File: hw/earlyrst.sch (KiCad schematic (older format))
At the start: 7 parts

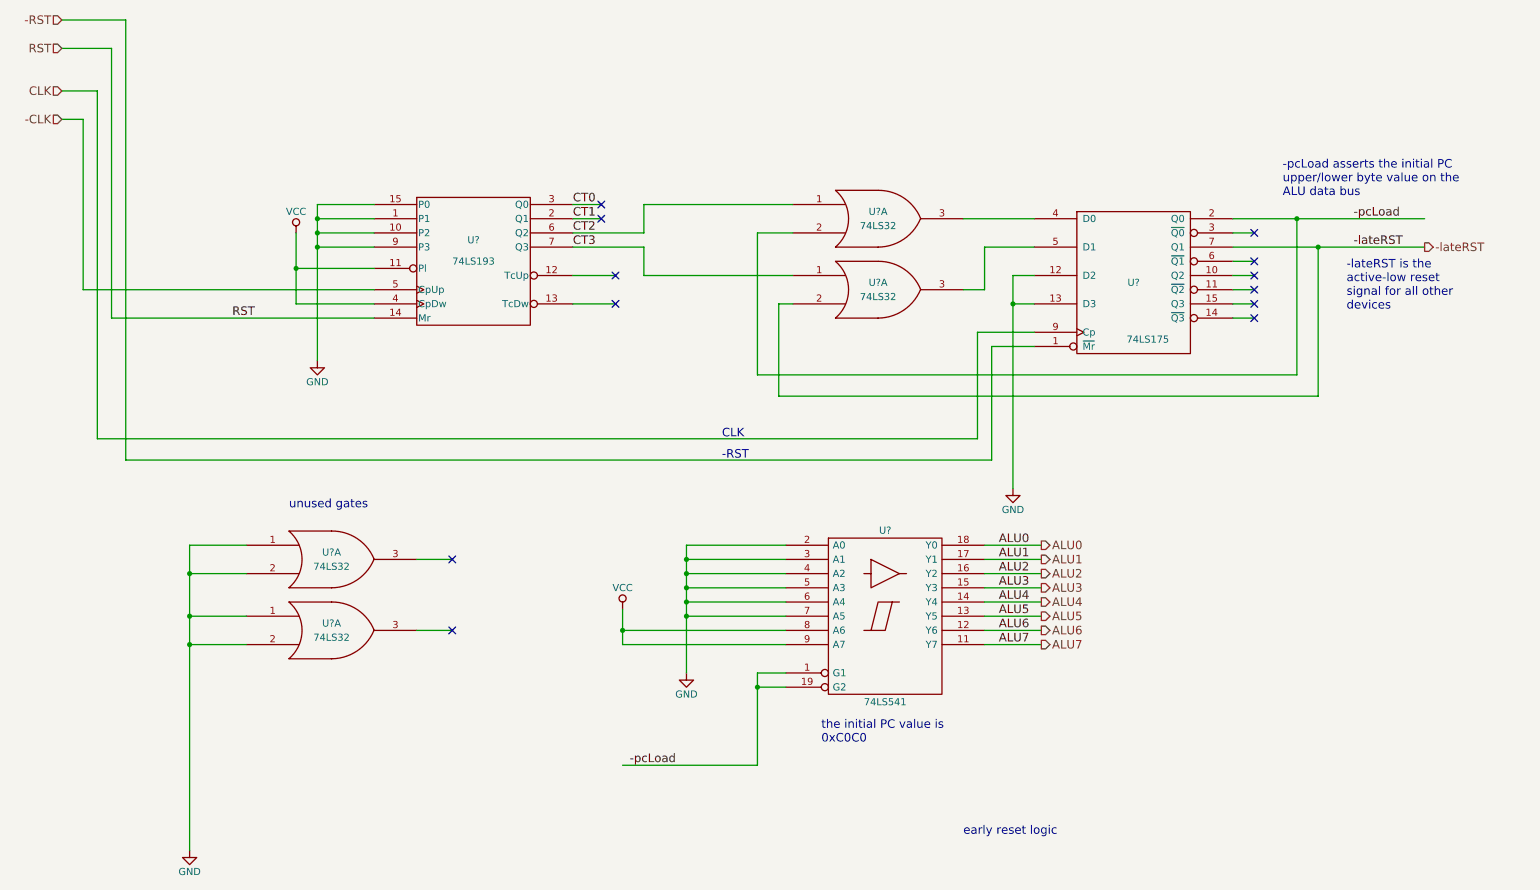
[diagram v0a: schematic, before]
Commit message: redesign of early reset logic
Use a '393 counter to generate delayed high signals for
-wrPC (write the PC high/low registers), -initPC
(assert the initial PC byte value on the ALU data bus),
and -lateRST (reset signal for other components.)

This (hopefully) fixes an issue with the previous design
where the initial PC value was clocked in on the same
clock edge as the one that de-asserted the driving of
the initial PC byte value onto the ALU data bus.
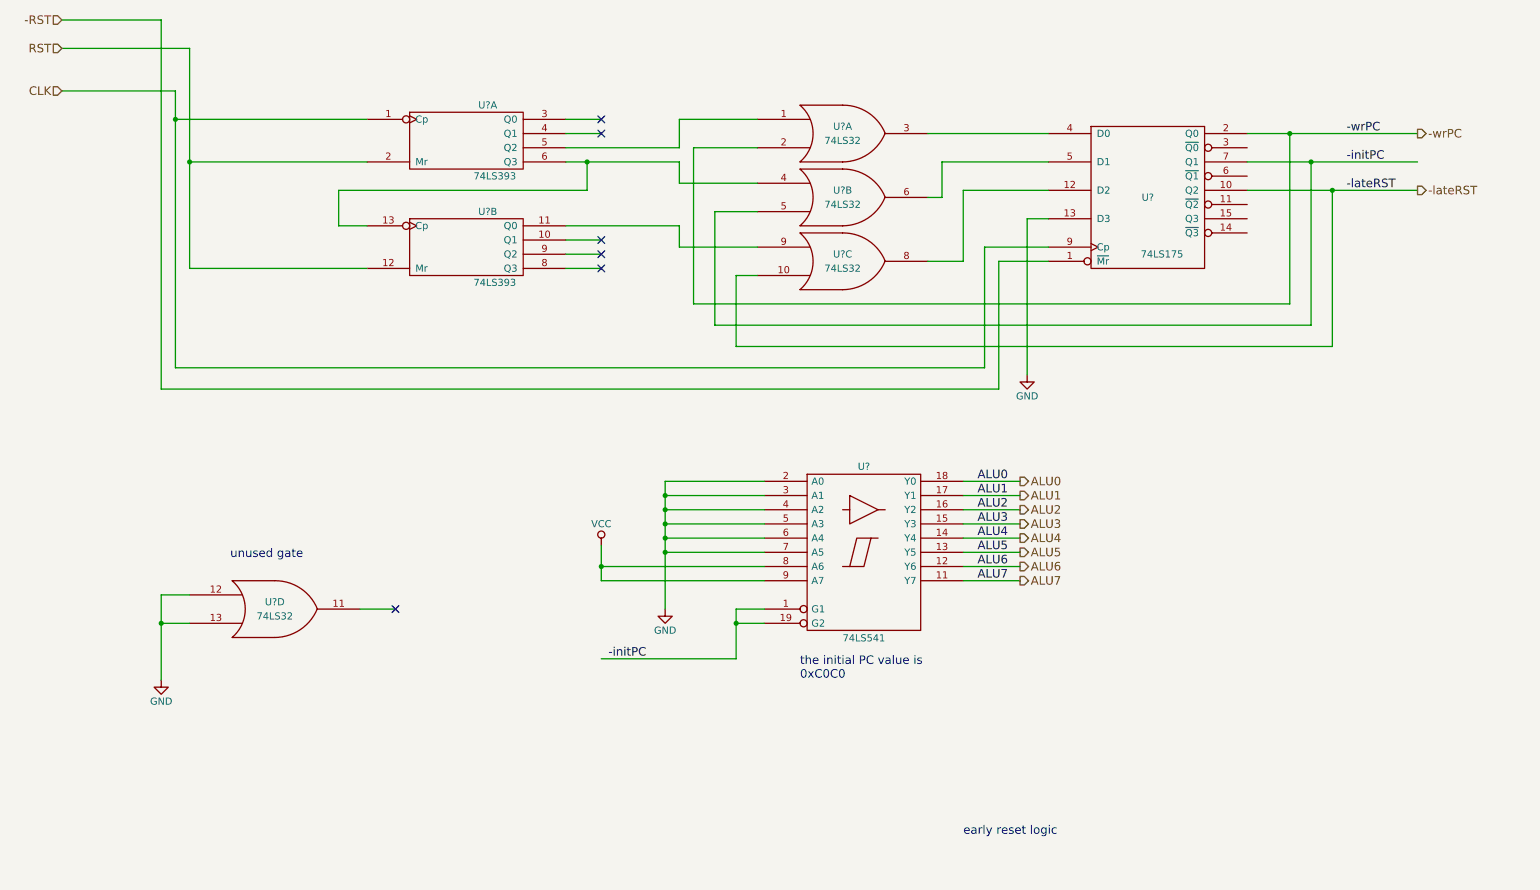
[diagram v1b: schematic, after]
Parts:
- removed U?: 74LS193, symbol 74LS193
- removed U? (x4): 74LS32, symbol 74LS32
- removed U?: 74LS175, symbol 74LS175
- added U? (x2): 74LS393, symbol 74LS393
- added U?: 74LS175, symbol 74LS175
- added U? (x4): 74LS32, symbol 74LS32
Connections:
- net -RST: now also U?.1 (~Mr)
- net -lateRST: now also U?.10, U?.10 (Q2)
- net CLK: now also U?.1 (Cp), U?.9 (Cp)
- net GND: now also U?.12, U?.13, U?.13 (D3), U?.7 (GND), U?.7 (GND), U?.7 (GND), U?.7 (GND), U?.7 (GND), U?.7 (GND), U?.8 (GND)
- net RST: now also U?.12 (Mr), U?.2 (Mr)
- net VCC: now also U?.14 (VCC), U?.14 (VCC), U?.14 (VCC), U?.14 (VCC), U?.14 (VCC), U?.14 (VCC), U?.16 (VCC)
- net -pcLoad renamed -initPC
- net -initPC: now also U?.5, U?.7 (Q1)
- new net: U?.1, U?.5 (Q2)
- new net: U?.13 (Cp), U?.4, U?.6 (Q3)
- new net: U?.11 (Q0), U?.9
- new net: U?.12 (D2), U?.8
- new net: U?.3, U?.4 (D0)
- new net: U?.5 (D1), U?.6
- new net -wrPC: U?.2, U?.2 (Q0)
- no-connect marks 12 -> 6
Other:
- note added: "unused gate"
- note removed: "-RST"
- note removed: "-lateRST is the\nactive-low reset\nsignal for all other\ndevices"
- note removed: "-pcLoad asserts the initial PC\nupper/lower byte value on the\nALU data bus"
- note removed: "CLK"
- note removed: "unused gates"
- moved on the sheet: U?
